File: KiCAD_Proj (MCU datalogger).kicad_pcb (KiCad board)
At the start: 2 copper layers, 0 parts

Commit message: Completed placement of footprints.
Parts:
- added BT1: Battery, Connector_PinHeader_2.54mm:PinHeader_1x02_P2.54mm_Vertical, F.Cu at (94.0, 85.1)
- added C1: 0.1uF, Capacitor_SMD:C_0805_2012Metric, F.Cu at (109.2, 78.7)
- added C2: 22pF, Capacitor_SMD:C_0805_2012Metric, F.Cu at (123.8, 94.0)
- added C3: 22pF, Capacitor_SMD:C_0805_2012Metric, F.Cu at (113.7, 78.7)
- added C4: 0.1uF, Capacitor_SMD:C_0805_2012Metric, F.Cu at (123.8, 97.8)
- added C5: 100nF, Capacitor_SMD:C_0805_2012Metric, F.Cu at (118.7, 78.7)
- added D1: LED, LED_SMD:LED_0805_2012Metric, F.Cu at (128.3, 78.7)
- added D2: LED, LED_SMD:LED_0805_2012Metric, F.Cu at (123.8, 78.7)
- added H1: MountingHole, MountingHole:MountingHole_2.1mm, F.Cu at (91.4, 78.7)
- added H2: MountingHole, MountingHole:MountingHole_2.1mm, F.Cu at (91.4, 104.1)
- added H3: MountingHole, MountingHole:MountingHole_2.1mm, F.Cu at (137.2, 78.7)
- added H4: MountingHole, MountingHole:MountingHole_2.1mm, F.Cu at (137.2, 104.1)
- added J1: Conn_01x04_Pin, Connector_PinHeader_2.54mm:PinHeader_1x04_P2.54mm_Vertical, F.Cu at (135.3, 92.1)
- added J2: Conn_01x09_Pin, Connector_PinHeader_2.54mm:PinHeader_1x09_P2.54mm_Vertical, F.Cu at (95.9, 103.5)
- added J3: Conn_01x04_Pin, Connector_PinHeader_2.54mm:PinHeader_1x04_P2.54mm_Vertical, F.Cu at (121.3, 103.5)
- added J4: Conn_02x03_Counter_Clockwise, Connector_PinHeader_2.54mm:PinHeader_2x03_P2.54mm_Vertical, F.Cu at (132.7, 83.2)
- added R1: 10K, Resistor_SMD:R_0805_2012Metric, F.Cu at (100.0, 99.1)
- added R2: 10K, Resistor_SMD:R_0805_2012Metric, F.Cu at (103.8, 99.1)
- added R3: 4.7K, Resistor_SMD:R_0805_2012Metric, F.Cu at (123.8, 90.2)
- added R4: 4.7K, Resistor_SMD:R_0805_2012Metric, F.Cu at (123.8, 86.4)
- added R5: 330, Resistor_SMD:R_0805_2012Metric, F.Cu at (128.3, 82.5)
- added R6: 10K, Resistor_SMD:R_0805_2012Metric, F.Cu at (128.3, 86.4)
- added R7: 330, Resistor_SMD:R_0805_2012Metric, F.Cu at (123.8, 82.5)
- added U1: 24LC1025-I_SM, 24LC1025-I_SM:SOIC127P794X202-8N, F.Cu at (101.6, 87.6)
- added U2: DS1337S_, DS1337S_:SOIC127P600X175-8N, F.Cu at (101.6, 94.6)
- added U3: 24LC1025-I_SM, 24LC1025-I_SM:SOIC127P794X202-8N, F.Cu at (101.6, 80.6)
- added U4: ATMEGA328P-AU, ATMEGA328P-AU:QFP80P900X900X120-32N, F.Cu at (114.3, 88.3)
- added Y1: 32.768 KHz, Crystal:Crystal_SMD_5032-2Pin_5.0x3.2mm_HandSoldering, F.Cu at (94.0, 95.9)
- added Y2: 16MHz, Crystal:Crystal_SMD_5032-2Pin_5.0x3.2mm_HandSoldering, F.Cu at (113.7, 97.2)
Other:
- board outline added: 50.8 x 30.5 mm

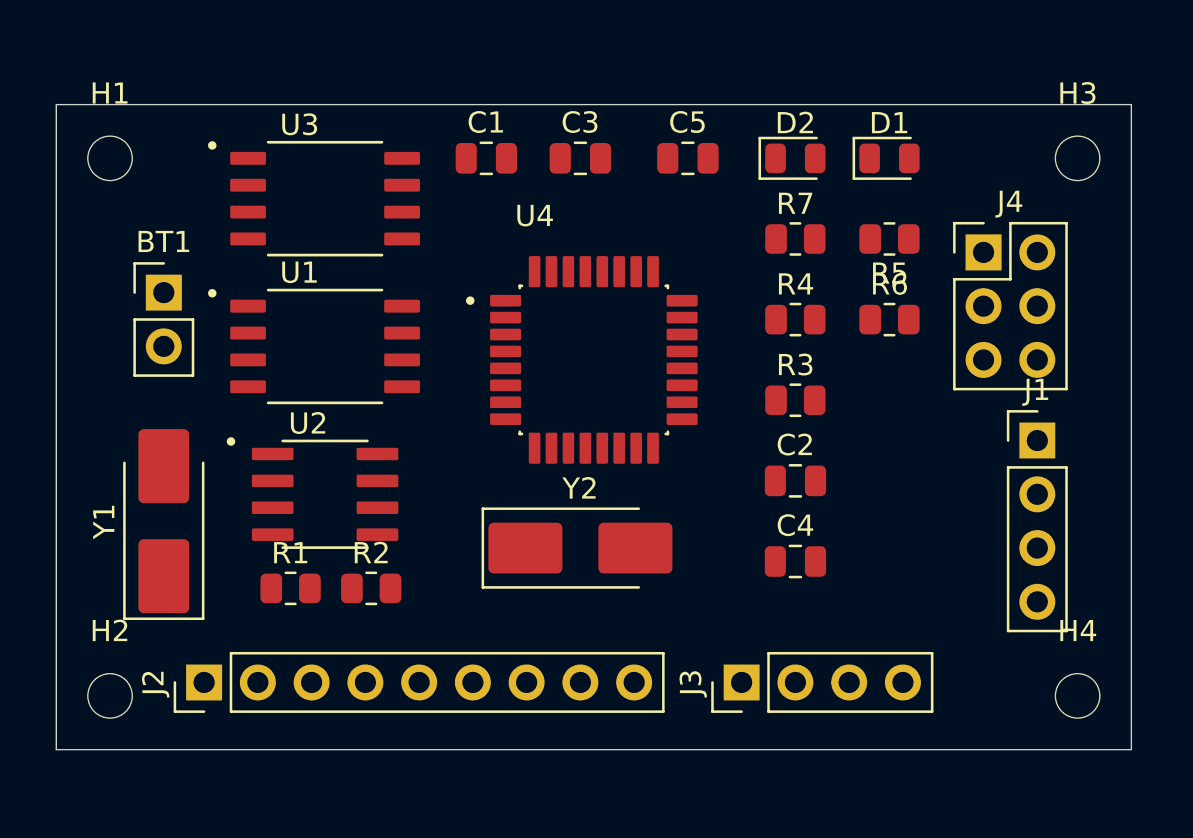
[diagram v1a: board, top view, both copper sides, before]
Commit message: Refined and completed outline
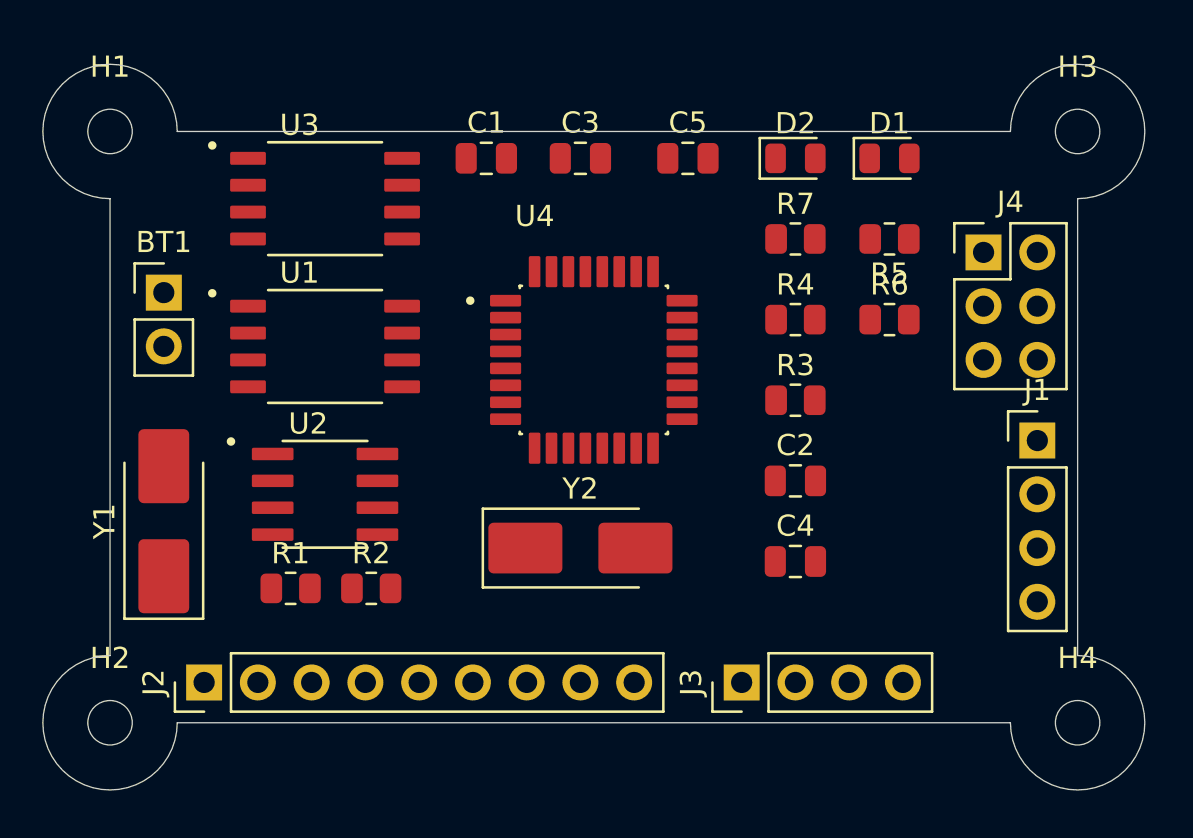
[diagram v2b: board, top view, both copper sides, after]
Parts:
- moved H1 1.27 mm to (91.4, 77.5)
- moved H2 1.27 mm to (91.4, 105.4)
- moved H3 1.27 mm to (137.2, 77.5)
- moved H4 1.27 mm to (137.2, 105.4)
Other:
- board size 50.8 x 30.5 mm -> 52.1 x 34.3 mm
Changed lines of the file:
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@@
 	(footprint "MountingHole:MountingHole_2.1mm"
 		(layer "F.Cu")
-		(at 91.44 104.14)
+		(at 91.44 105.41)
 		(descr "Mounting Hole 2.1mm, no annular, generated by kicad-footprint-generator mountinghole.py")
 		(tags "mountinghole")
@@
 	(footprint "MountingHole:MountingHole_2.1mm"
 		(layer "F.Cu")
-		(at 137.16 104.14)
+		(at 137.16 105.41)
 		(descr "Mounting Hole 2.1mm, no annular, generated by kicad-footprint-generator mountinghole.py")
 		(tags "mountinghole")
@@
 	(footprint "MountingHole:MountingHole_2.1mm"
 		(layer "F.Cu")
-		(at 137.16 78.74)
+		(at 137.16 77.47)
 		(descr "Mounting Hole 2.1mm, no annular, generated by kicad-footprint-generator mountinghole.py")
 		(tags "mountinghole")
@@
 	(footprint "MountingHole:MountingHole_2.1mm"
 		(layer "F.Cu")
-		(at 91.44 78.74)
+		(at 91.44 77.47)
 		(descr "Mounting Hole 2.1mm, no annular, generated by kicad-footprint-generator mountinghole.py")
 		(tags "mountinghole")
@@
 		(embedded_fonts no)
 	)
-	(gr_rect
-		(start 88.9 76.2)
-		(end 139.7 106.68)
+	(gr_line
+		(start 91.44 102.235)
+		(end 91.44 80.645)
+		(stroke
+			(width 0.05)
+			(type default)
+		)
+		(layer "Edge.Cuts")
+	)
+	(gr_line
+		(start 133.985 105.41)
+		(end 94.615 105.41)
+		(stroke
+			(width 0.05)
+			(type default)
+		)
+		(layer "Edge.Cuts")
+	)
+	(gr_arc
+		(start 94.615 105.41)
+		(mid 89.194936 107.655064)
+		(end 91.44 102.235)
+		(stroke
+			(width 0.05)
+			(type default)
+		)
+		(layer "Edge.Cuts")
+	)
+	(gr_arc
+		(start 91.44 80.645)
+		(mid 89.194936 75.224936)
+		(end 94.615 77.47)
+		(stroke
+			(width 0.05)
+			(type default)
+		)
+		(layer "Edge.Cuts")
+	)
+	(gr_line
+		(start 94.615 77.47)
+		(end 133.985 77.47)
+		(stroke
+			(width 0.05)
+			(type default)
+		)
+		(layer "Edge.Cuts")
+	)
+	(gr_arc
+		(start 137.16 102.235)
+		(mid 139.405064 107.655064)
+		(end 133.985 105.41)
+		(stroke
+			(width 0.05)
+			(type default)
+		)
+		(layer "Edge.Cuts")
+	)
+	(gr_arc
+		(start 133.985 77.47)
+		(mid 139.405064 75.224936)
+		(end 137.16 80.645)
+		(stroke
+			(width 0.05)
+			(type default)
+		)
+		(layer "Edge.Cuts")
+	)
+	(gr_line
+		(start 137.16 80.645)
+		(end 137.16 102.235)
 		(stroke
 			(width 0.05)
 			(type default)
 		)
-		(fill no)
 		(layer "Edge.Cuts")
 	)

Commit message: Routing sans GND Vcc Complete.
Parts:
- moved J3 1.27 mm to (122.6, 103.5)
- moved J2 1.27 mm to (97.2, 103.5)
- turned C2 to 180 degrees
- turned C4 to 180 degrees
- turned R2 to 180 degrees
- turned R3 to 180 degrees
- turned R4 to 180 degrees
- turned Y2 to 180 degrees
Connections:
- BT1 pad 1: /Vcc -> Net-(BT1-+)
- C5 pad 1: /Vcc -> Net-(BT1-+)
- D2 pad 2: /Vcc -> Net-(BT1-+)
- J4 pad 2: /SCK -> /Vcc
- J4 pad 3: /RESET -> /SCK
- J4 pad 4: GND -> /MOSI
- J4 pad 5: /MOSI -> /RESET
- J4 pad 6: /Vcc -> GND
- U4 pad 18: /Vcc -> Net-(BT1-+)
- U4 pad 4: /Vcc -> Net-(BT1-+)
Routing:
- net /SCK: track 0.00 -> 97.0 mm, vias 0 -> 3
- net /Vcc: track 0.00 -> 95.6 mm, vias 0 -> 1
- net Net-(BT1-+): track 0.00 -> 60.0 mm, vias 0 -> 5
- net /SDA: track 0.00 -> 57.3 mm, vias 0 -> 2
- net GND: track 0.00 -> 50.8 mm, vias 0 -> 6
- net /TX: track 0.00 -> 32.1 mm, vias 0 -> 1
- net /RX: track 0.00 -> 28.6 mm, vias 0 -> 1
- net Net-(U4-PB7): track 0.00 -> 28.4 mm, vias 0 -> 2
- net /D2: track 0.00 -> 26.3 mm, vias 0 -> 1
- net Net-(U4-PB6): track 0.00 -> 25.0 mm
- net /MOSI: track 0.00 -> 24.9 mm
- net /D3: track 0.00 -> 24.7 mm
- net /RESET: track 0.00 -> 23.5 mm, vias 0 -> 4
- net /D4: track 0.00 -> 22.4 mm
- net /MISO: track 0.00 -> 20.3 mm, vias 0 -> 1
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
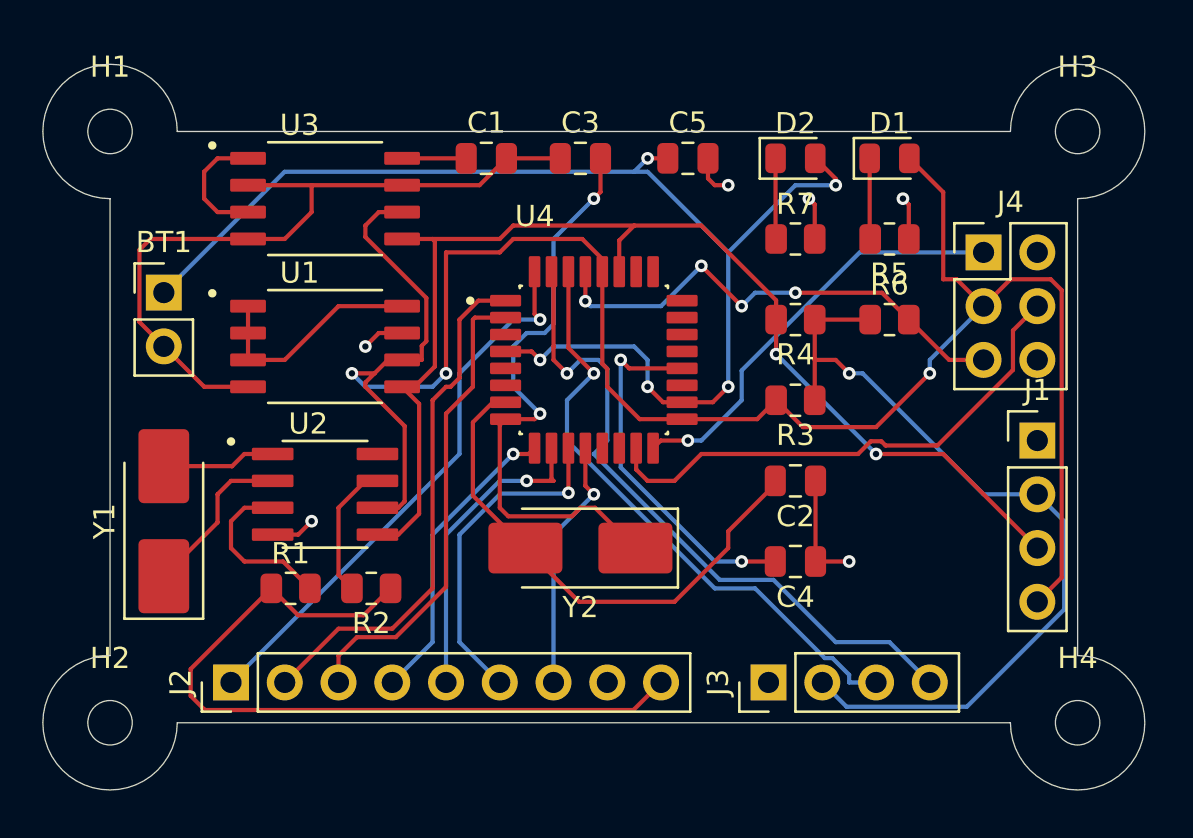
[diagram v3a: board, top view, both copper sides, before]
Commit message: Routing sans GND Vcc complete.
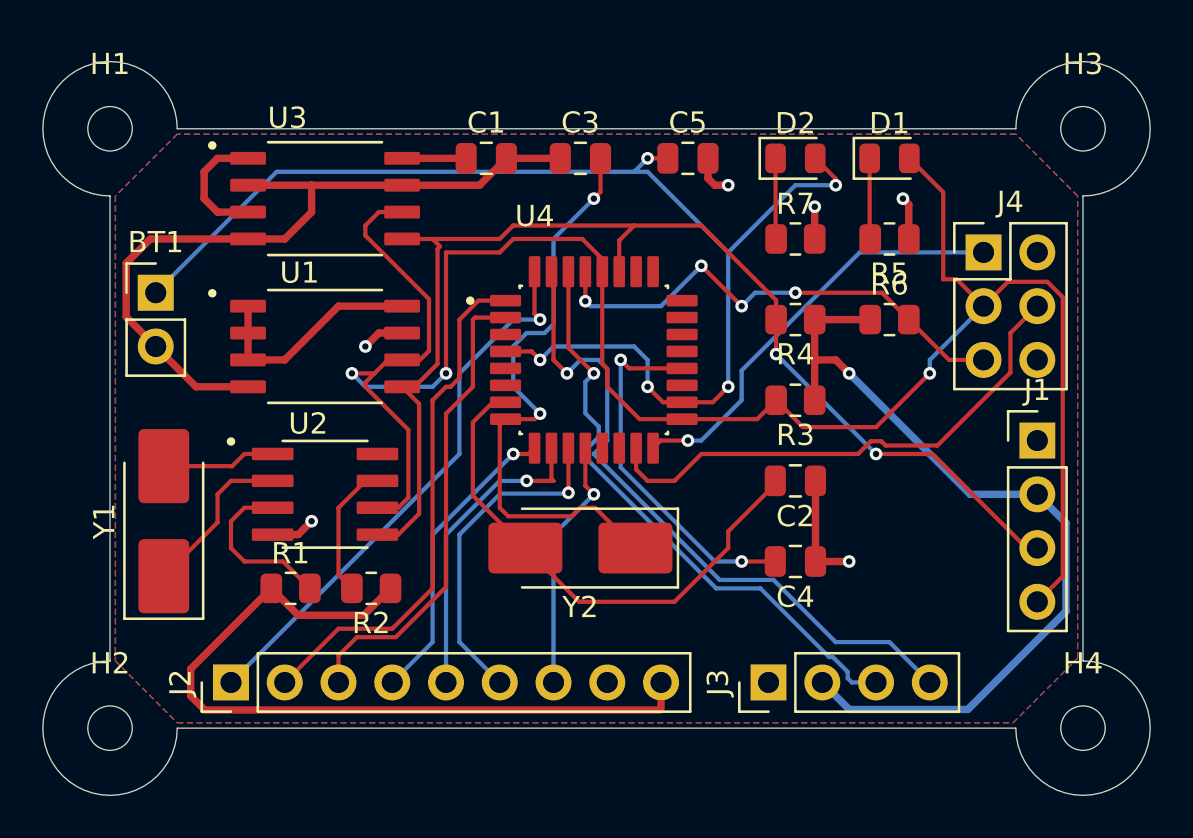
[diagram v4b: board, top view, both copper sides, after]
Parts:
- moved BT1 0.38 mm to (93.6, 85.1)
- moved H4 0.36 mm to (137.4, 105.7)
- moved H3 0.28 mm to (137.4, 77.3)
- moved H2 0.25 mm to (91.4, 105.7)
- moved H1 0.13 mm to (91.4, 77.3)
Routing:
- net /Vcc: track 95.6 -> 96.6 mm
- added copper zone on F.Cu, net /Vcc
- added copper zone on B.Cu, net GND
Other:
- board size 52.1 x 34.3 mm -> 52.3 x 34.7 mm

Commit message: Refined routing complete.
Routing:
- net GND: track 51.1 -> 84.2 mm, vias 6 -> 12
- net /Vcc: track 96.6 -> 118.3 mm, vias 1 -> 5
- net /D2: track 26.3 -> 29.8 mm
- net /D3: track 24.7 -> 26.8 mm, vias 0 -> 2
- net Net-(U4-AREF): track 17.3 -> 18.0 mm
- net /SCK: track 96.9 -> 97.6 mm
- net /RX: track 28.3 -> 27.6 mm
- net /D4: track 22.4 -> 23.1 mm, vias 0 -> 2
- net Net-(U4-PB6): track 25.0 -> 25.5 mm

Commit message: Fixed outstanding issues.
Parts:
- added G***: LOGO, LOGO, B.Cu at (101.2, 87.6)
- added REF**: KiCad-Logo2_5mm_SilkScreen, Symbol:KiCad-Logo2_5mm_SilkScreen, B.Cu at (101.6, 80.9)
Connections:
- BT1 pad 1: Net-(BT1-+) -> /Vcc
- C5 pad 1: Net-(BT1-+) -> /Vcc
- D2 pad 2: Net-(BT1-+) -> /Vcc
- U4 pad 18: Net-(BT1-+) -> /Vcc
- U4 pad 4: Net-(BT1-+) -> /Vcc
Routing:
- net /Vcc: track 118.3 -> 178.7 mm, vias 5 -> 10
- net Net-(BT1-+): track 60.4 -> 0.00 mm, vias 5 -> 0
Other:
- board text added: "0.0000 mm / 0.0000 mm"
- board text added: "0.1uF"
- board text added: "0.3000 mm"
- board text added: "1.6000 mm"
- board text added: "100nF"
- board text added: "10K"
- board text added: "16 MHz"
- board text added: "2"
- board text added: "22pF"
- board text added: "24LC1025"
- board text added: "3"
- board text added: "32.768 KHz"
- board text added: "330"
- board text added: "4"
- board text added: "4.7K"
- board text added: "5"
- board text added: "52.3190 mm x 34.6660 mm"
- board text added: "6"
- board text added: "7"
- board text added: "8"
- board text added: "ATMEGA328P-AU"
- board text added: "BOARD CHARACTERISTICS"
- board text added: "Battery"
- board text added: "Board Thickness:"
- board text added: "Board overall dimensions:"
- board text added: "Castellated pads:"
- board text added: "Copper Finish:"
- board text added: "Copper Layer Count:"
- board text added: "Data logger with the ATMega328P. - 2Mbit EEPROM - RTC - I2C, SPI, GPIOs"
- board text added: "Edge card connectors:"
- board text added: "GND"
- board text added: "GPIO"
- board text added: "I2C"
- board text added: "ICSP"
- board text added: "ISCP"
- board text added: "Impedance Control:"
- board text added: "LED"
- board text added: "MISO"
- board text added: "MOSI"
- board text added: "Min hole diameter:"
- board text added: "Min track/spacing:"
- board text added: "No"
- board text added: "None"
- board text added: "Plated Board Edge:"
- board text added: "RESET"
- board text added: "RX"
- board text added: "SCK"
- board text added: "SDA"
- board text added: "SERIAL"
- board text added: "TX"
- board text added: "VCC"
- board text added: "| | |"
